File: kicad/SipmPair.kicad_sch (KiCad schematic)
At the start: 26 parts, among them J12 Conn_Coaxial, J13 Conn_Coaxial, U12 OPA847IDBVT, U13 OPA847IDBVT

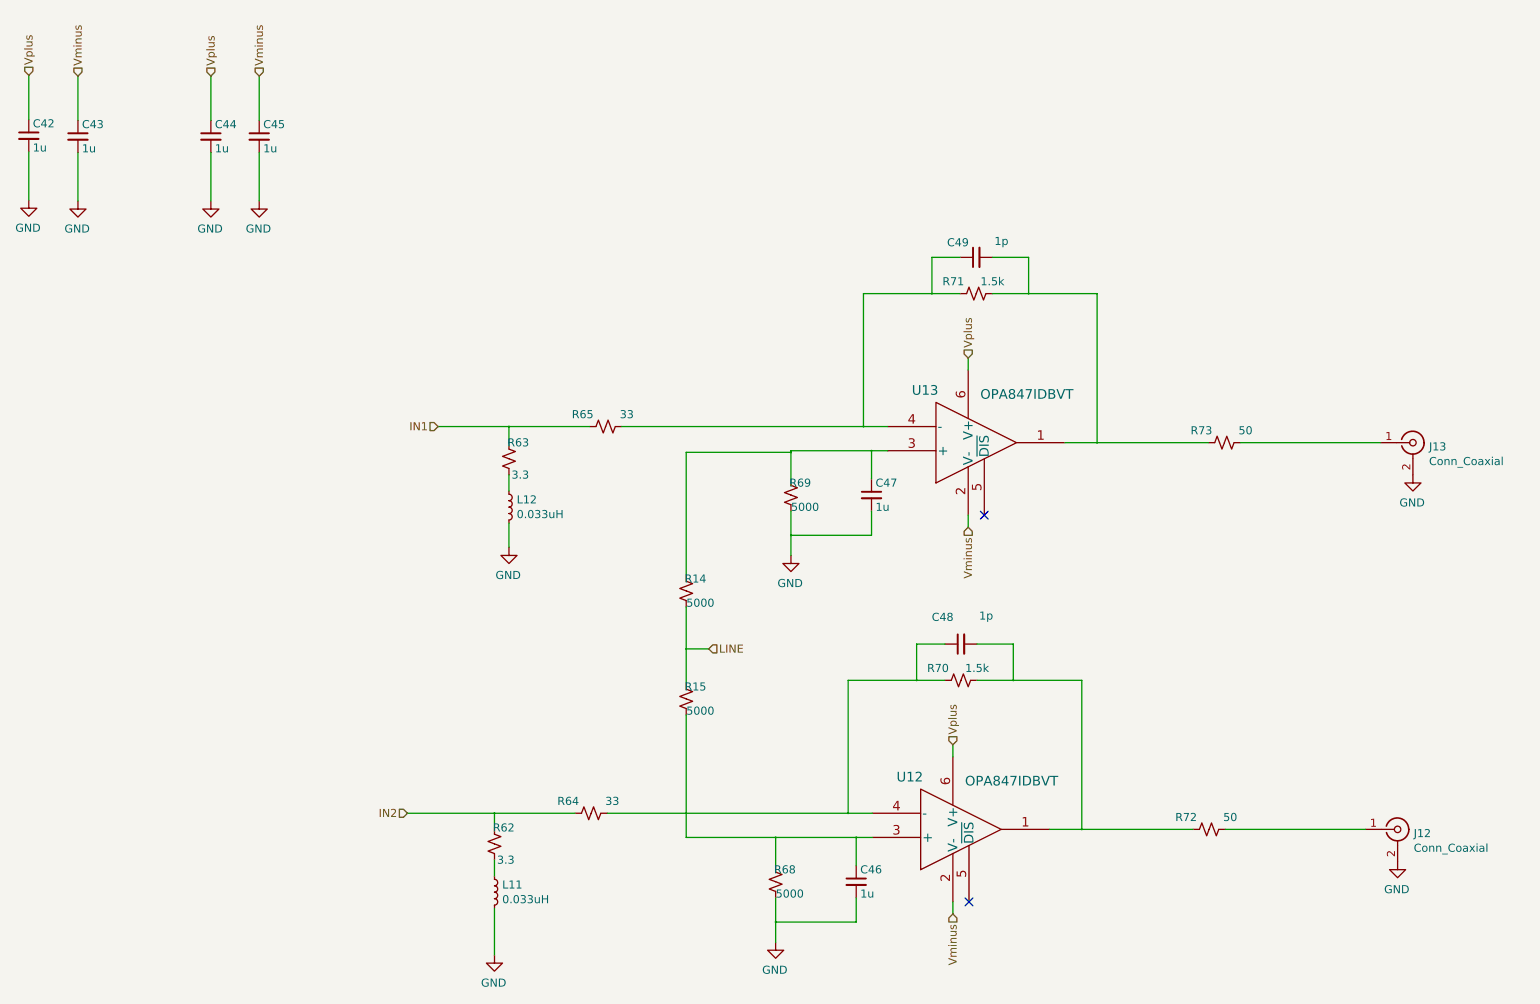
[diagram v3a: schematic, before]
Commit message: Check in before removing feedback cap
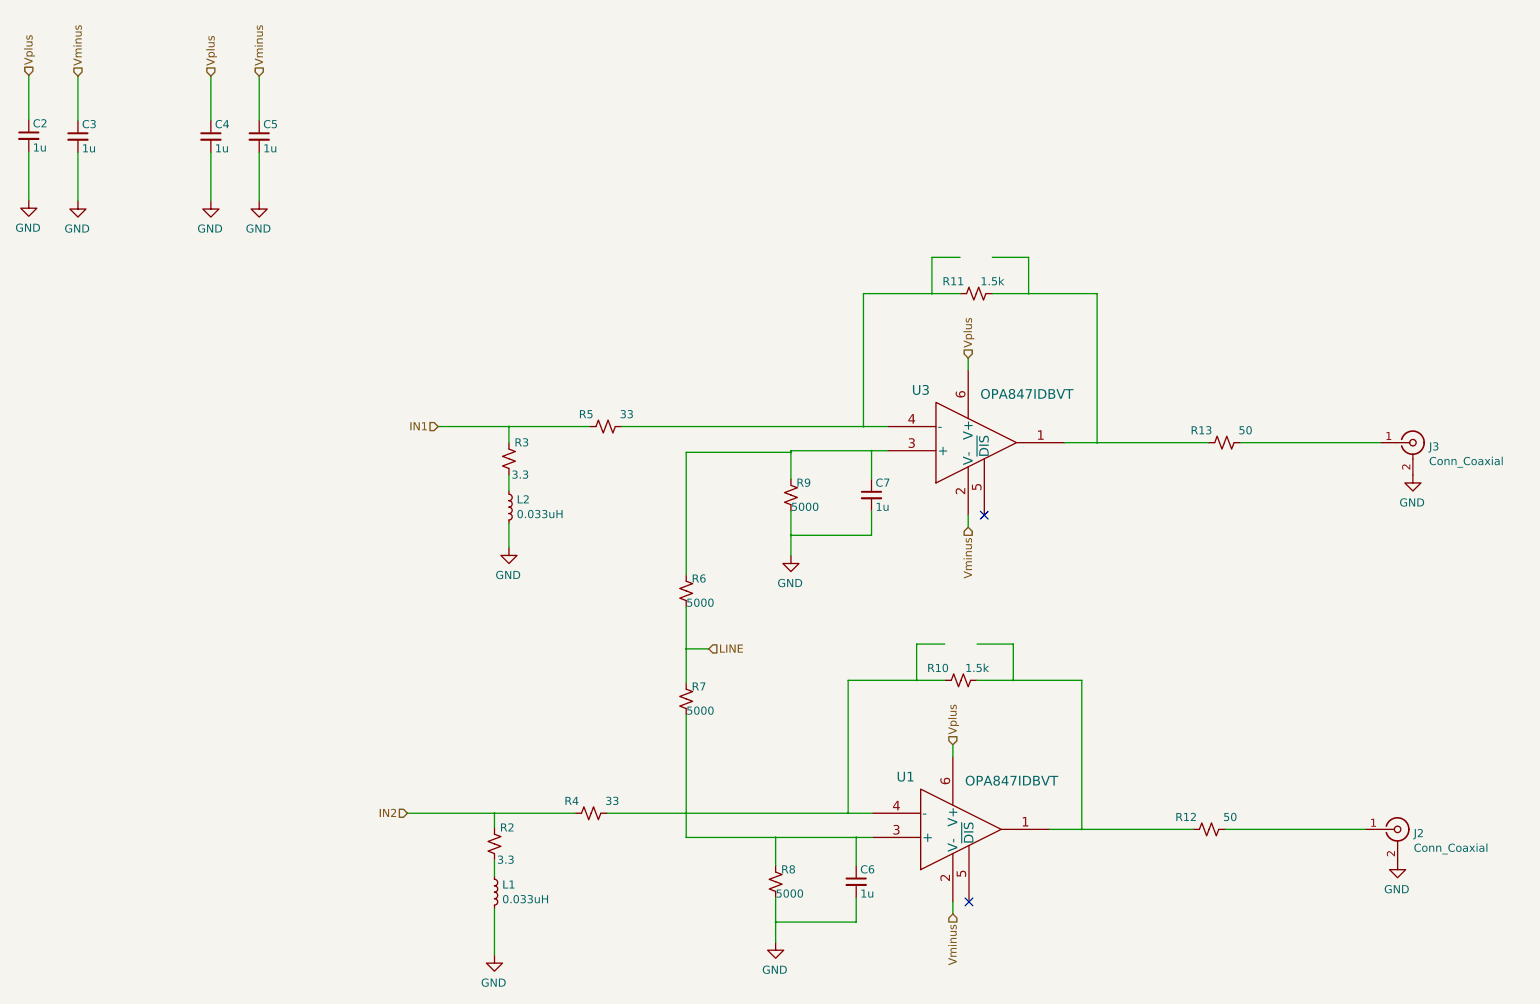
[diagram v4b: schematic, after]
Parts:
- removed C48, C49: 1p, C_0402_1005Metric, symbol Device:C_Small
- renumbered C42 to C2, C43 to C3, C44 to C4, C45 to C5, C46 to C6, C47 to C7, J12 to J2, J13 to J3, L11 to L1, L12 to L2, R70 to R10, R71 to R11, R72 to R12, R73 to R13, R62 to R2, R63 to R3, R64 to R4, R65 to R5, R14 to R6, R15 to R7, R68 to R8, R69 to R9, U12 to U1, U13 to U3

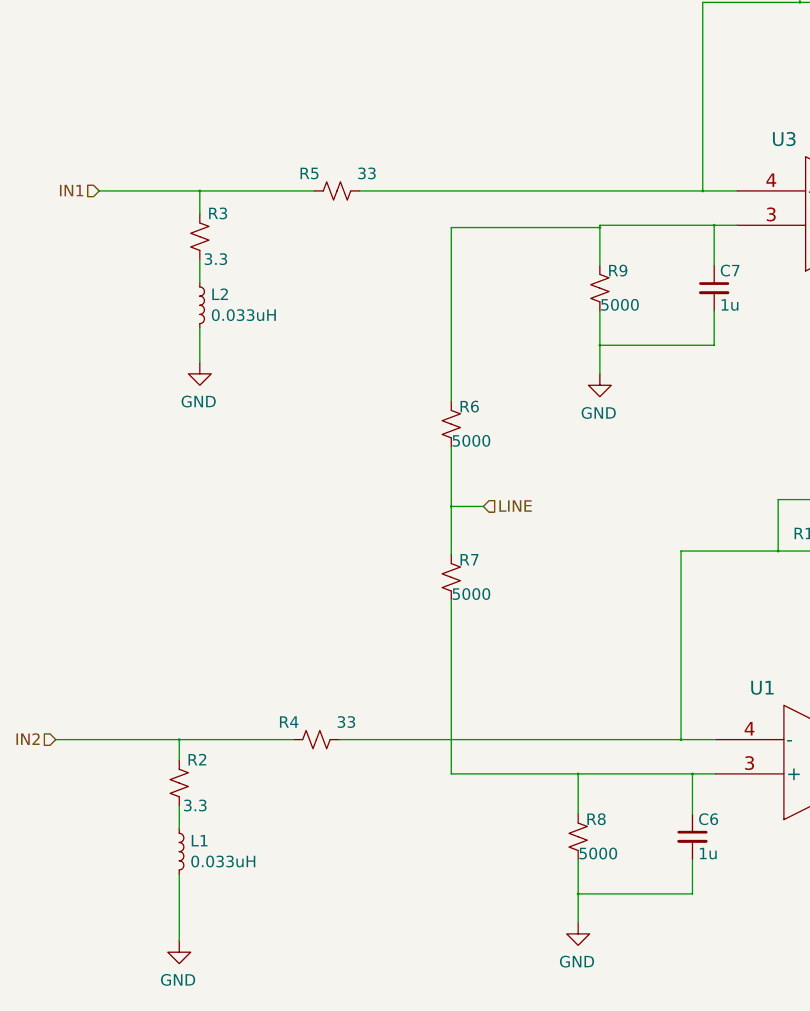
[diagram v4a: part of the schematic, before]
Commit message: Update the PCB with final PZC and offset values
In testing, the PZC worked well with 6.3/43/90nH on the S14160-1315 which we are assuming is very similar.  These values may not be quite right for the array but are hopefully close.  The 68/5000 ohm offset divider also seemed optimal on the single sipm.
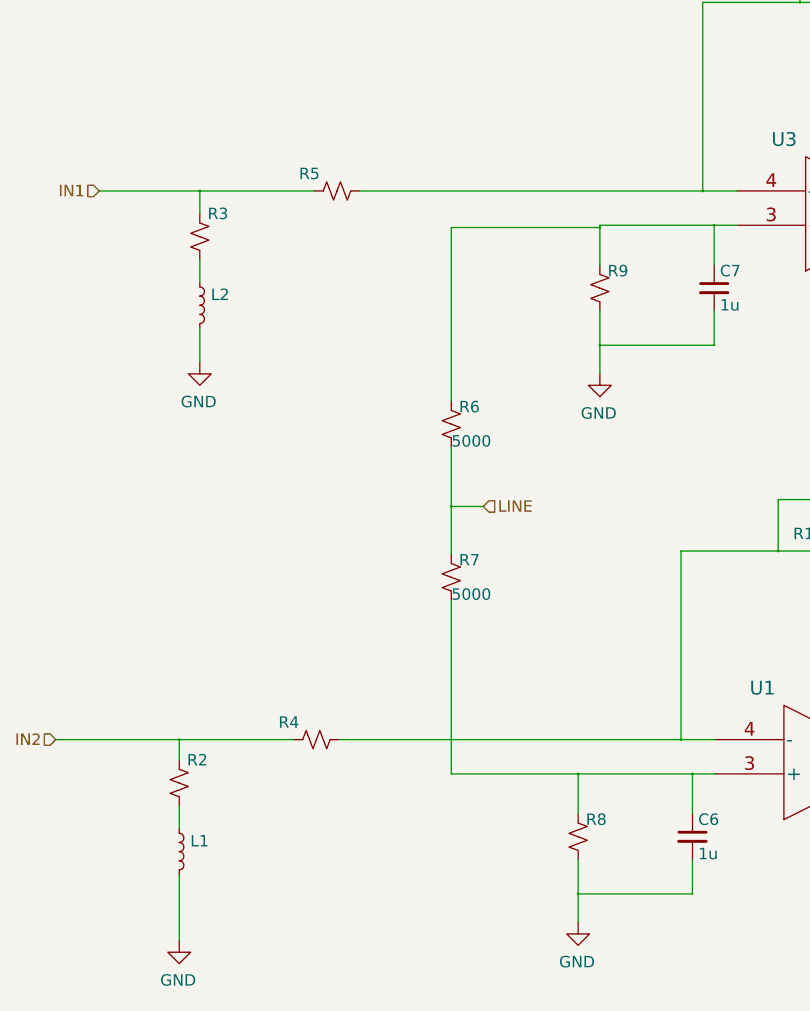
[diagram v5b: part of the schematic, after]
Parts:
- L1, L2: value 0.033uH -> (none); footprint footprints:C_0402_1005Metric -> (none)
- R2, R3: value 3.3 -> (none)
- R4, R5: value 33 -> (none); footprint R_0402_1005Metric -> (none)
- R8: value 5000 -> (none); footprint R_0402_1005Metric -> (none)
- R9: value 5000 -> (none)

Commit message: Change decoupling to 1206
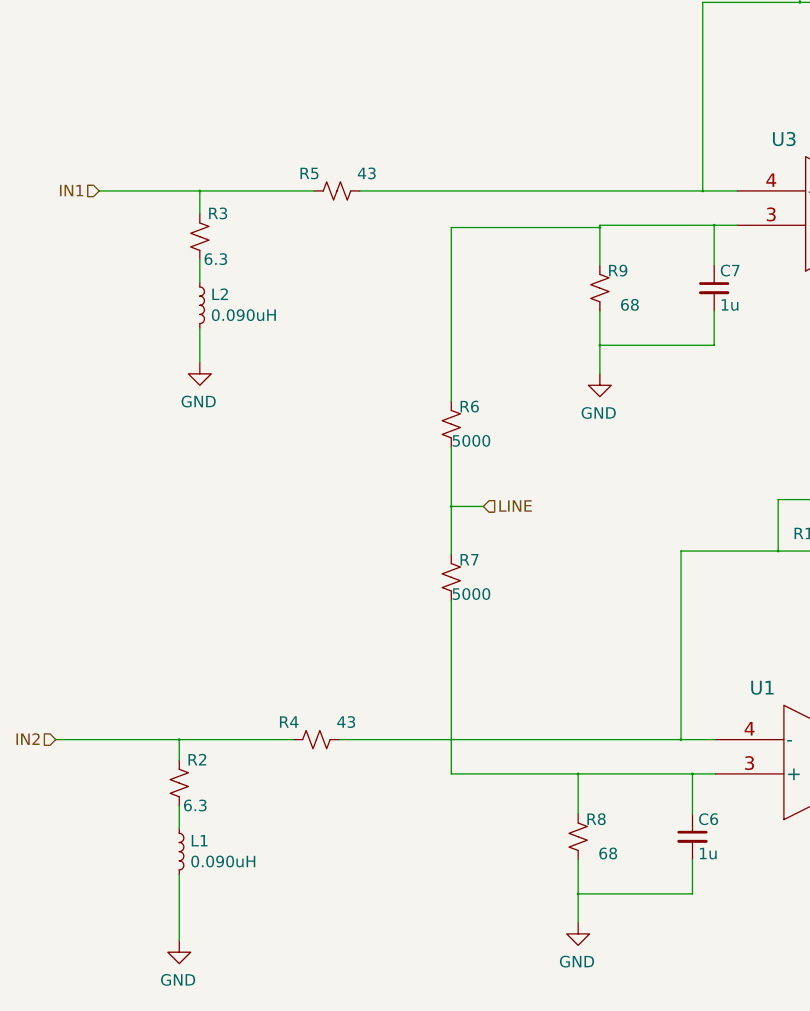
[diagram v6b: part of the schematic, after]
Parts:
- L1, L2: value (none) -> 0.090uH; footprint (none) -> footprints:C_0402_1005Metric
- R2, R3: value (none) -> 6.3
- R4, R5: value (none) -> 43; footprint (none) -> R_0402_1005Metric
- R8: value (none) -> 68; footprint (none) -> R_0402_1005Metric
- R9: value (none) -> 68
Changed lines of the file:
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@@
       (effects (font (size 1.27 1.27)) (justify left))
     )
-    (property "Value" "" (id 1) (at 105.359 93.853 0)
-      (effects (font (size 1.27 1.27)) (justify left))
-    )
-    (property "Footprint" "" (id 2) (at 104.14 92.71 0)
+    (property "Value" "0.090uH" (id 1) (at 105.359 93.853 0)
+      (effects (font (size 1.27 1.27)) (justify left))
+    )
+    (property "Footprint" "footprints:C_0402_1005Metric" (id 2) (at 104.14 92.71 0)
       (effects (font (size 1.27 1.27)) hide)
     )
@@
       (effects (font (size 1.27 1.27)) (justify left))
     )
-    (property "Value" "" (id 1) (at 107.315 87.63 0)
+    (property "Value" "6.3" (id 1) (at 107.315 87.63 0)
       (effects (font (size 1.27 1.27)) (justify left))
     )
@@
       (effects (font (size 1.27 1.27)) (justify left))
     )
-    (property "Value" "" (id 1) (at 103.073 154.559 0)
-      (effects (font (size 1.27 1.27)) (justify left))
-    )
-    (property "Footprint" "" (id 2) (at 101.854 153.416 0)
+    (property "Value" "0.090uH" (id 1) (at 103.073 154.559 0)
+      (effects (font (size 1.27 1.27)) (justify left))
+    )
+    (property "Footprint" "footprints:C_0402_1005Metric" (id 2) (at 101.854 153.416 0)
       (effects (font (size 1.27 1.27)) hide)
     )
@@
       (effects (font (size 1.27 1.27)) (justify left))
     )
-    (property "Value" "" (id 1) (at 150.622 153.67 0)
-      (effects (font (size 1.27 1.27)) (justify left))
-    )
-    (property "Footprint" "" (id 2) (at 146.177 151.765 0)
+    (property "Value" "68" (id 1) (at 150.622 153.67 0)
+      (effects (font (size 1.27 1.27)) (justify left))
+    )
+    (property "Footprint" "R_0402_1005Metric" (id 2) (at 146.177 151.765 0)
       (effects (font (size 1.27 1.27)) hide)
     )
@@
       (effects (font (size 1.27 1.27)) (justify left))
     )
-    (property "Value" "" (id 1) (at 121.539 139.065 90)
-      (effects (font (size 1.27 1.27)) (justify left))
-    )
-    (property "Footprint" "" (id 2) (at 117.094 140.97 0)
+    (property "Value" "43" (id 1) (at 121.539 139.065 90)
+      (effects (font (size 1.27 1.27)) (justify left))
+    )
+    (property "Footprint" "R_0402_1005Metric" (id 2) (at 117.094 140.97 0)
       (effects (font (size 1.27 1.27)) hide)
     )
@@
       (effects (font (size 1.27 1.27)) (justify left))
     )
-    (property "Value" "" (id 1) (at 105.029 148.336 0)
+    (property "Value" "6.3" (id 1) (at 105.029 148.336 0)
       (effects (font (size 1.27 1.27)) (justify left))
     )
@@
       (effects (font (size 1.27 1.27)) (justify left))
     )
-    (property "Value" "" (id 1) (at 153.035 92.71 0)
+    (property "Value" "68" (id 1) (at 153.035 92.71 0)
       (effects (font (size 1.27 1.27)) (justify left))
     )
@@
       (effects (font (size 1.27 1.27)) (justify left))
     )
-    (property "Value" "" (id 1) (at 123.825 78.105 90)
-      (effects (font (size 1.27 1.27)) (justify left))
-    )
-    (property "Footprint" "" (id 2) (at 119.38 80.01 0)
-      (effects (font (size 1.27 1.27)) hide)
-    )
+    (property "Value" "43" (id 1) (at 123.825 78.105 90)
+      (effects (font (size 1.27 1.27)) (justify left))
+    )
+    (property "Footprint" "R_0402_1005Metric" (id 2) (at 119.38 80.01 0)
+      (effects (font (size 1.27 1.27)) hide)
+    )

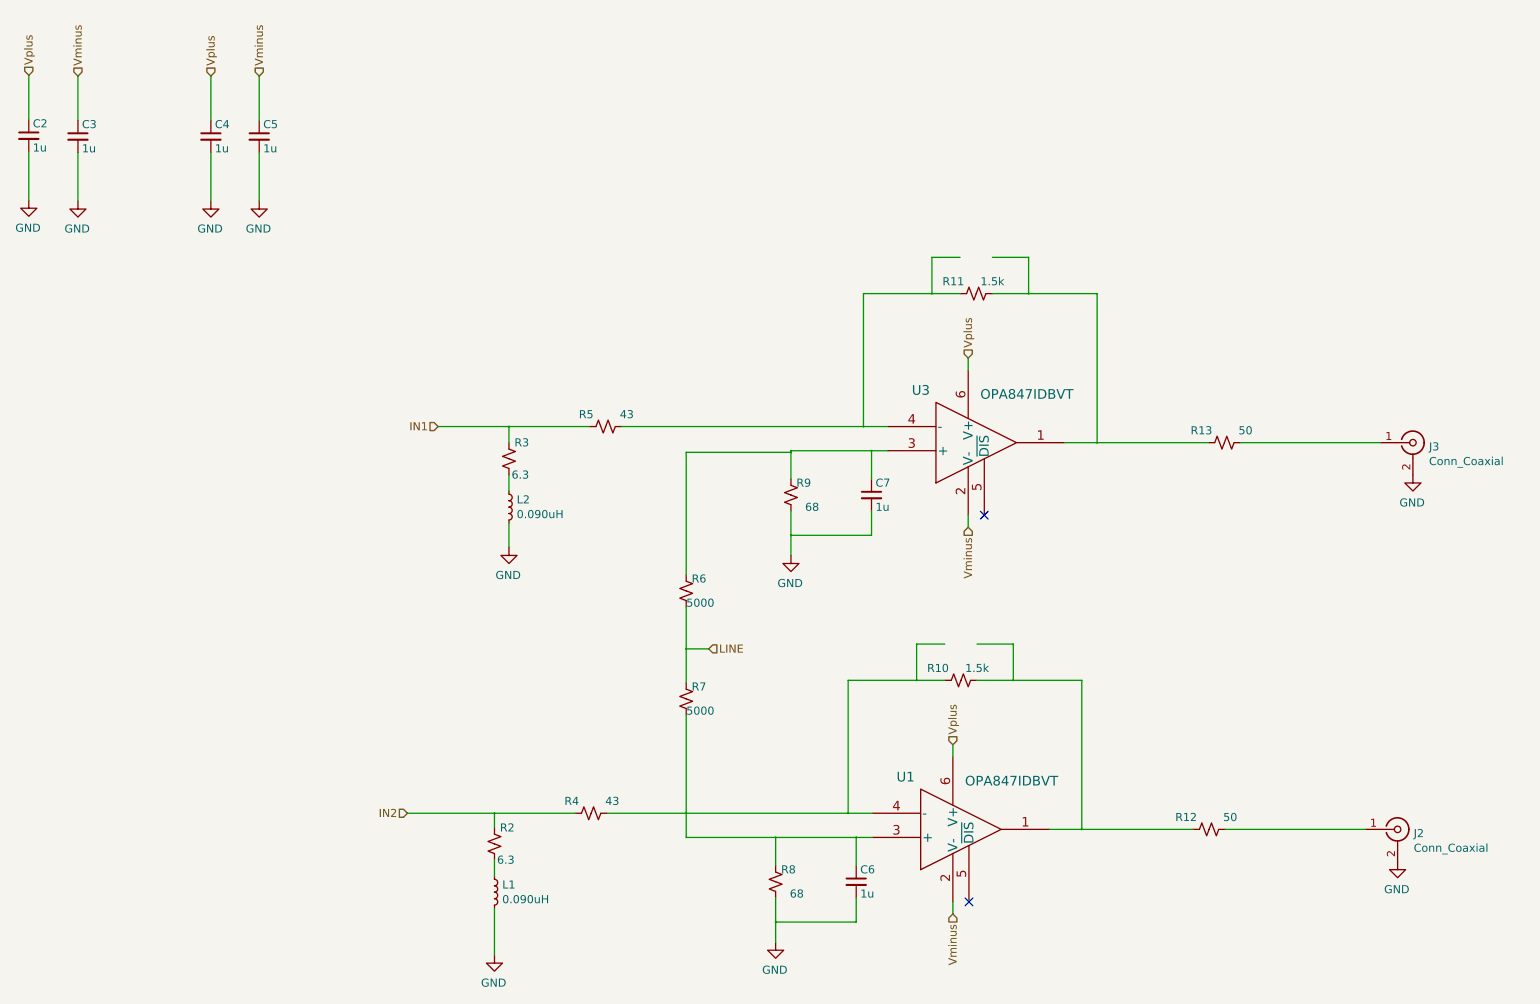
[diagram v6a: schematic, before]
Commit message: Fix track under drill hole
Pretty sure JLCPCB quietly fixed this for us on the initial design.
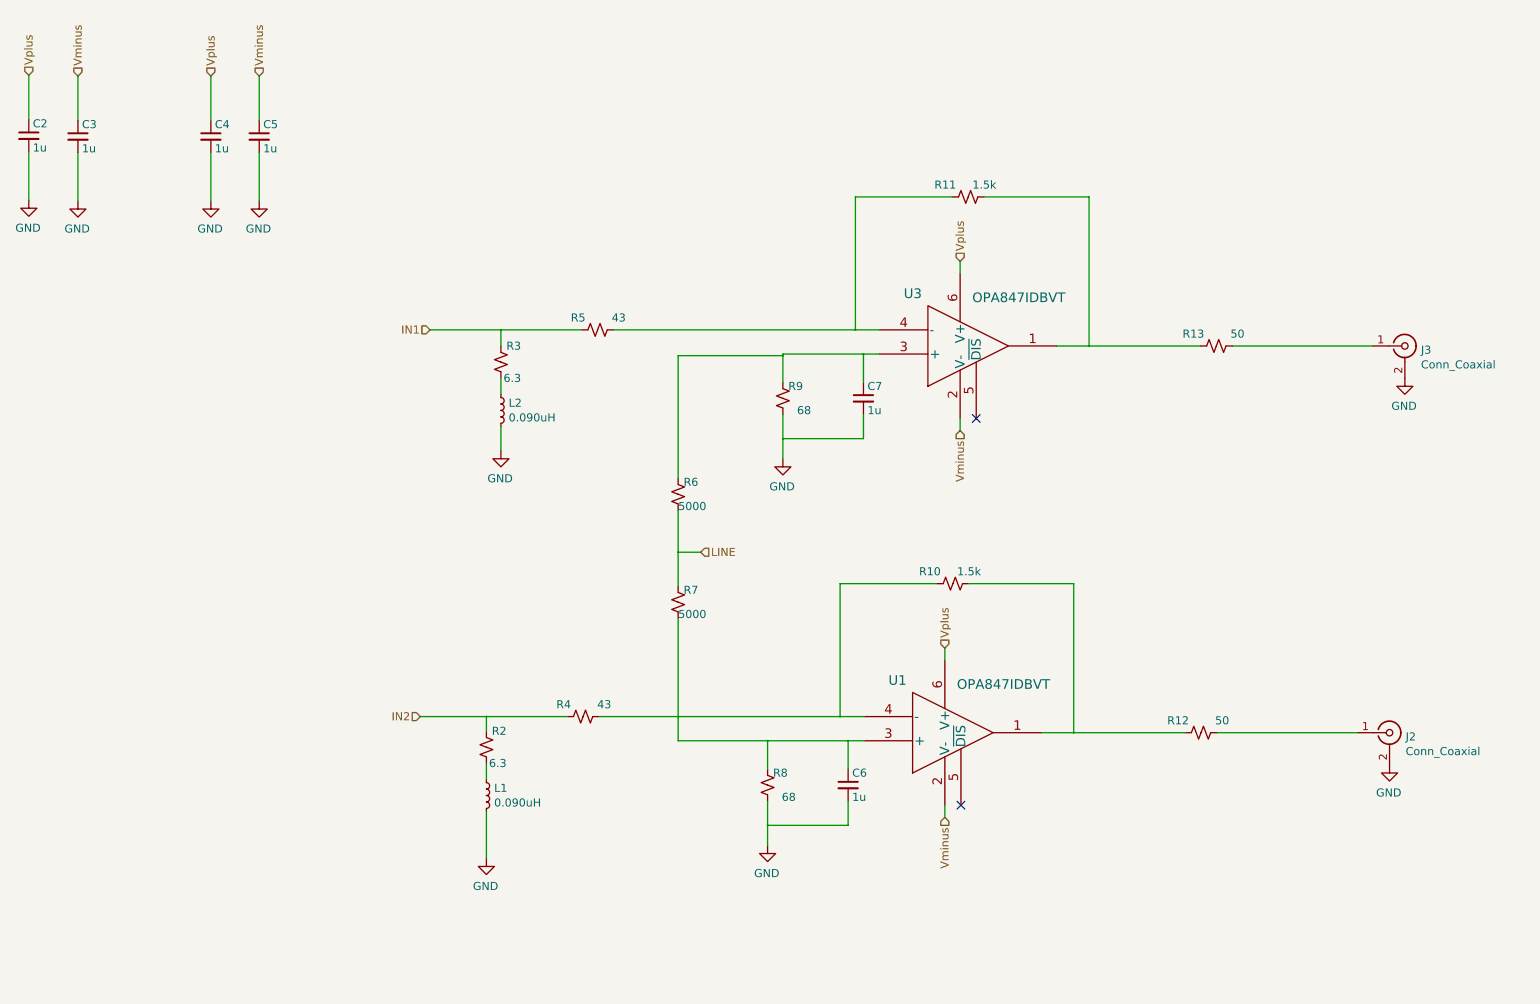
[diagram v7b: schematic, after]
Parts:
- C2, C3, C4, C5, C6, C7: Voltage (none) -> 16V
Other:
- moved on the sheet: C6, C7, J2, J3, L1, L2, R10, R11, R12, R13, R2, R3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
